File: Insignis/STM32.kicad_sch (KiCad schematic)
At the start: 24 parts, among them IC7 STM32F405OGY6VTR, Y2 32.768kHz, Y4 Crystal_GND24

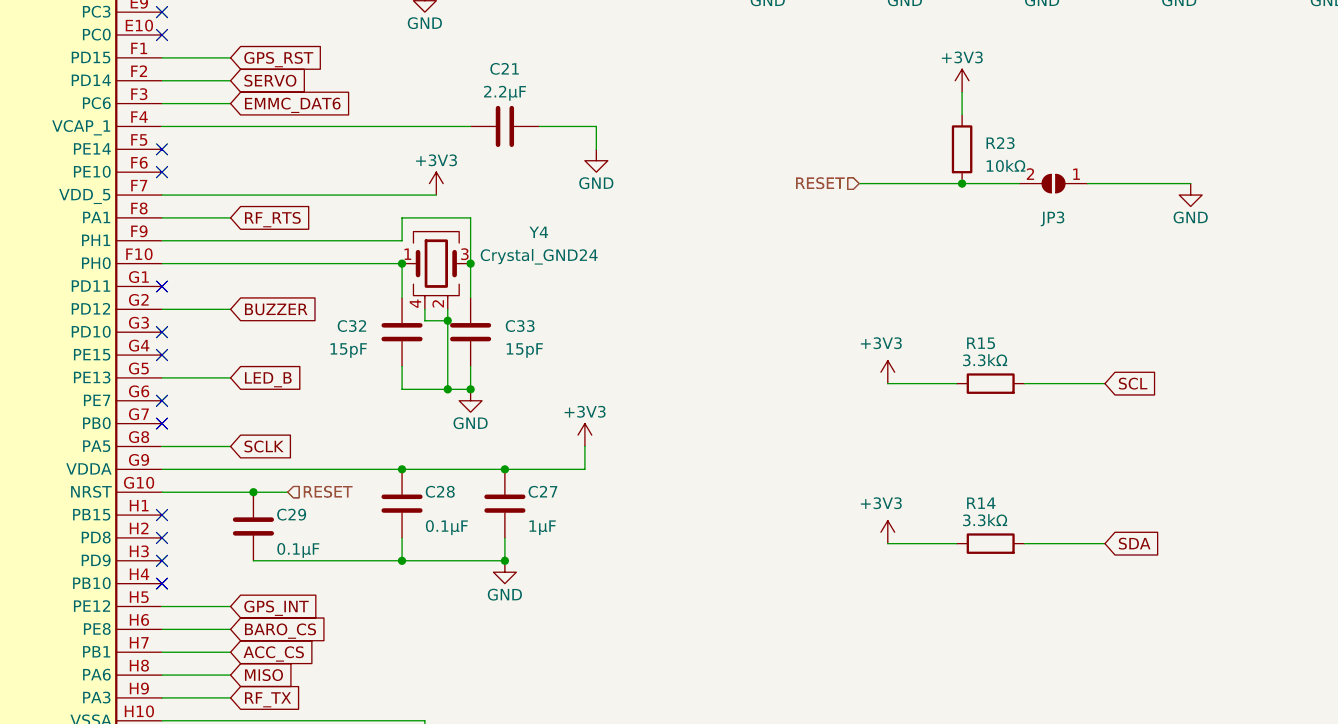
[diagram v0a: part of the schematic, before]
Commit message: Fixed ERC errors
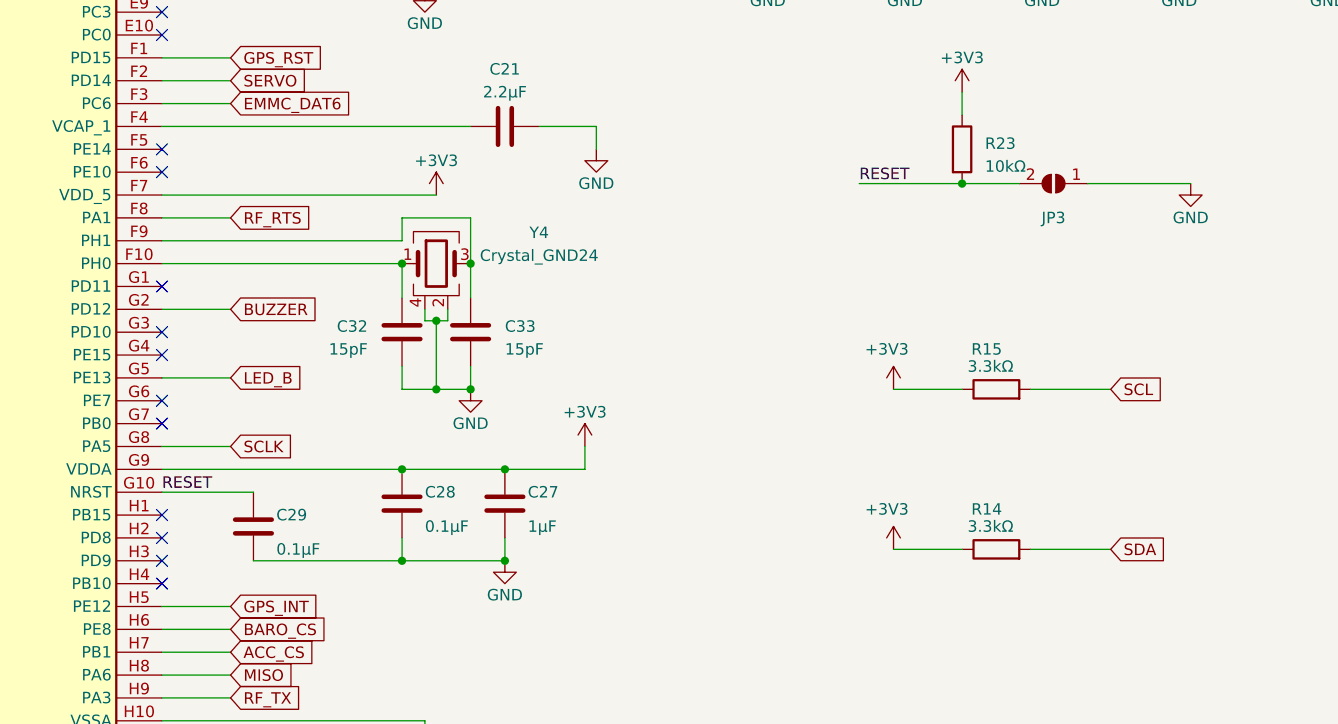
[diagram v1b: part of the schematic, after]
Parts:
- IC7: footprint BGA90C40P10X9_422X397X60 -> STM32F405OGY6VTR:BGA90C40P10X9_422X397X60
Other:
- moved on the sheet: R14, R15
